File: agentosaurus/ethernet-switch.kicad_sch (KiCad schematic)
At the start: 19 parts, among them T1 HX1188NL, U1 RTL8367S, Y1 25MHz

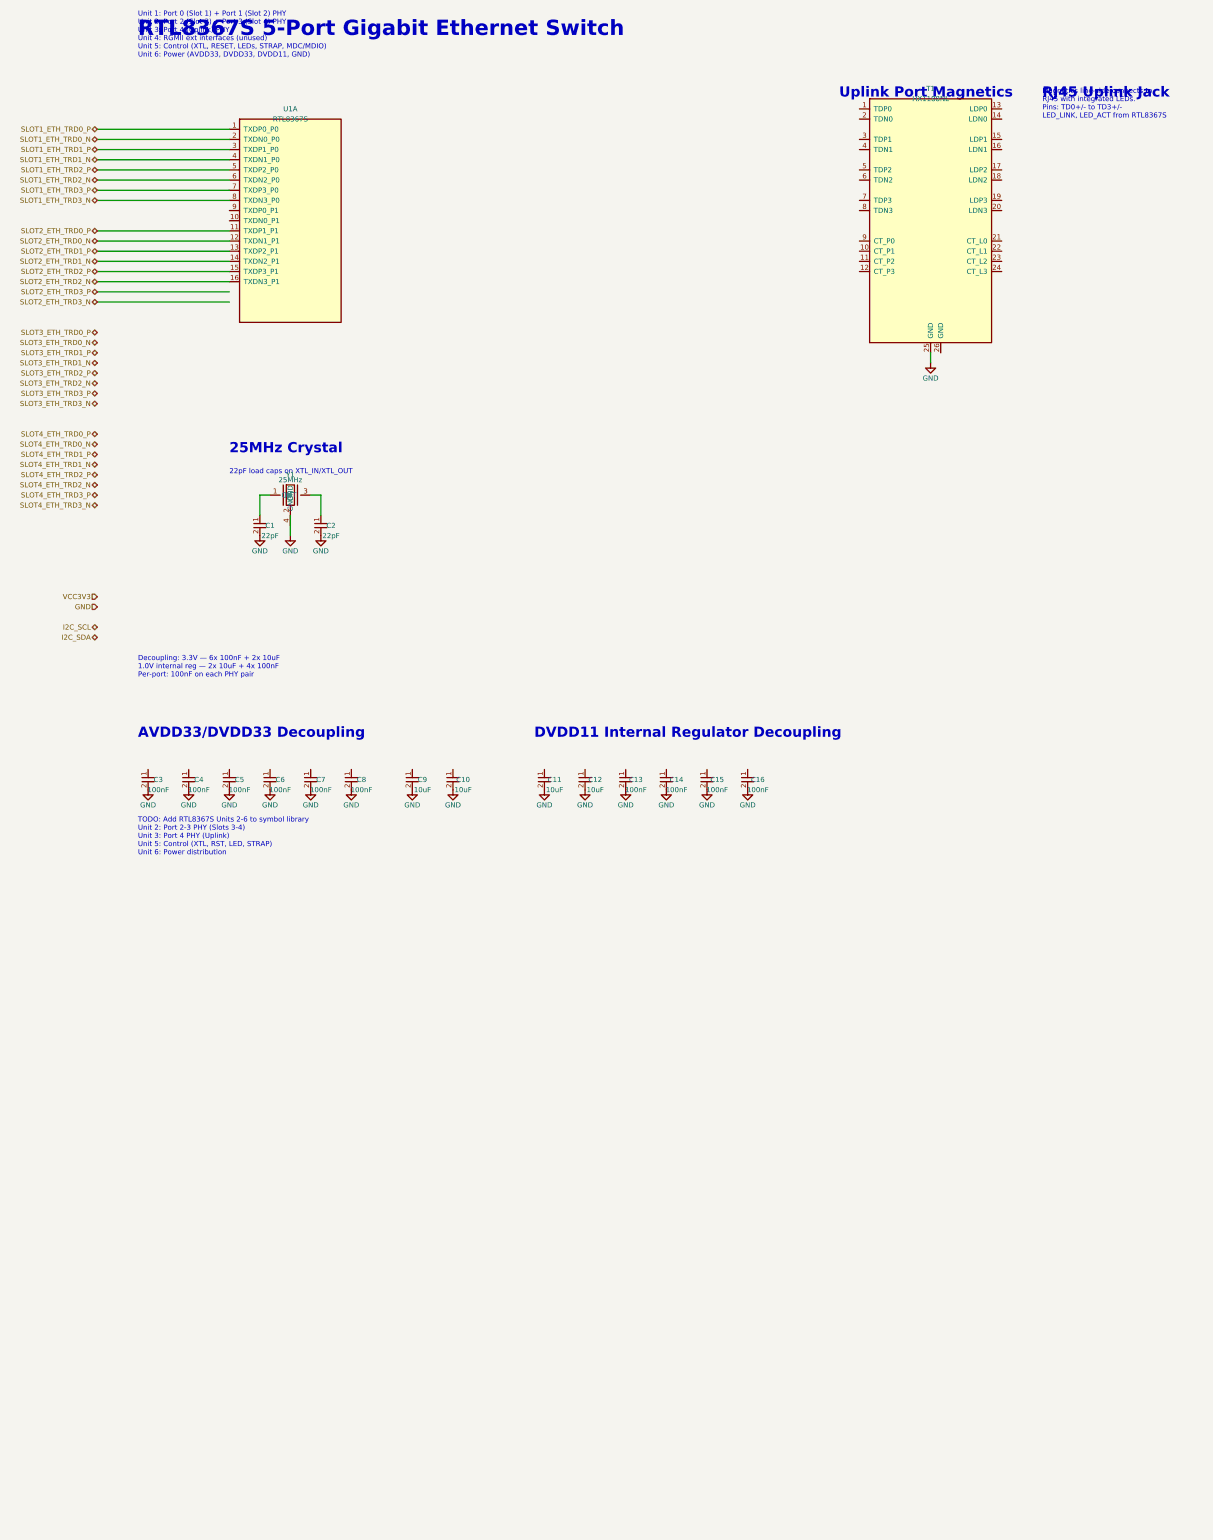
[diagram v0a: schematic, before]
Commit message: Add RTL8367S Units 2-6 with full wiring to ethernet switch
- Unit 2 (Ports 2-3 PHY): Slots 3-4 ethernet connections
- Unit 3 (Port 4 PHY): Uplink magnetics T1 connections
- Unit 5 (Control): MDC/MDIO to I2C, XTL to crystal, reset pull-up,
  strap pins to GND, MNG_MODE pull-up for SMI mode
- Unit 6 (Power): AVDD33/DVDD33 to VCC3V3, DVDD11 internal reg,
  AGND/DGND to GND
- Remove TODO text annotation

https://claude.ai/code/session_01UhhXLgEHsAy83XEALyNrDb
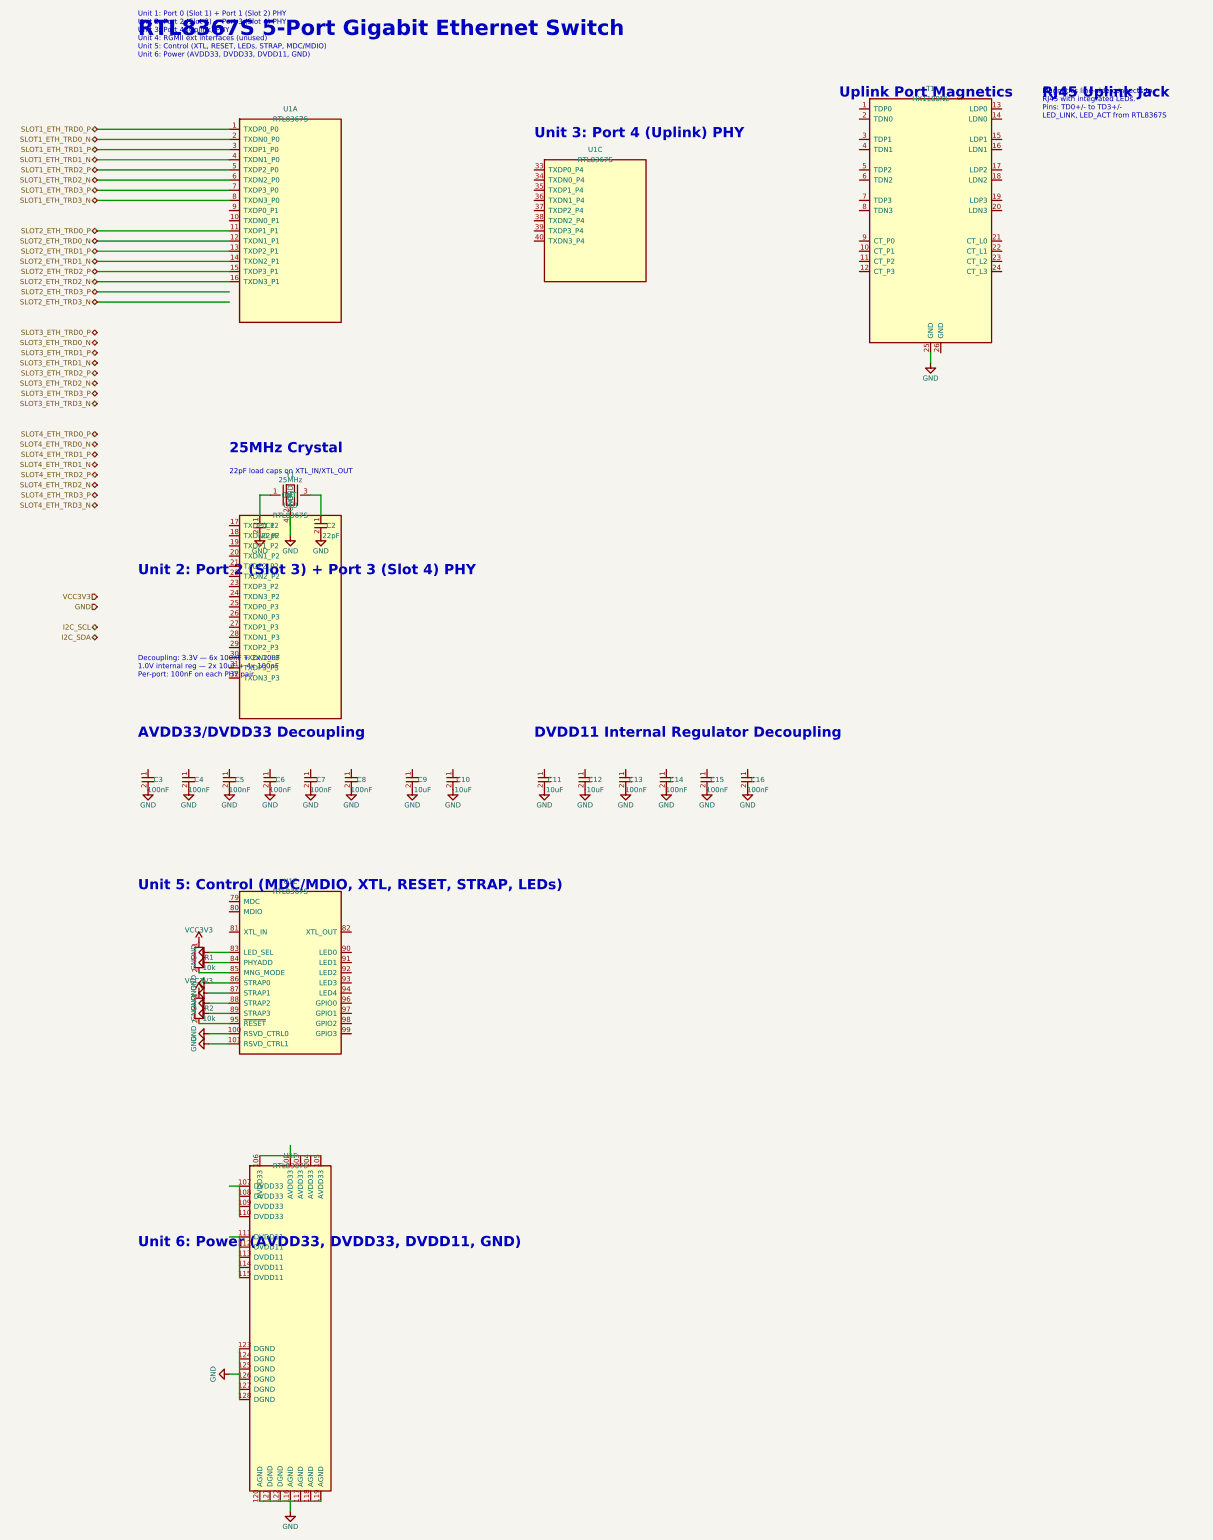
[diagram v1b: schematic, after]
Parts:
- added R1, R2: 10k, Resistor_SMD:R_0402_1005Metric, symbol Device:R
- added unit 2 of U1
- added unit 3 of U1
- added unit 5 of U1
- added unit 6 of U1
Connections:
- net GND: now also U1.100 (RSVD_CTRL0), U1.101 (RSVD_CTRL1), U1.116 (AGND), U1.83 (LED_SEL), U1.84 (PHYADD), U1.86 (STRAP0), U1.87 (STRAP1), U1.88 (STRAP2), U1.89 (STRAP3)
- net VCC3V3: now also R1.1, R2.1
- new net: R1.2, U1.85 (MNG_MODE)
- new net: R2.2, U1.95 (~{RESET})
- new net: U1.105 (AVDD33), U1.106 (AVDD33)
- new net: U1.107 (DVDD33), U1.110 (DVDD33)
- new net: U1.111 (DVDD11), U1.115 (DVDD11)
- new net: U1.119 (AGND), U1.120 (AGND)
- new net: U1.123 (DGND), U1.128 (DGND)
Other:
- note added: "Unit 2: Port 2 (Slot 3) + Port 3 (Slot 4) PHY"
- note added: "Unit 3: Port 4 (Uplink) PHY"
- note added: "Unit 5: Control (MDC/MDIO, XTL, RESET, STRAP, LEDs)"
- note added: "Unit 6: Power (AVDD33, DVDD33, DVDD11, GND)"
- note removed: "TODO: Add RTL8367S Units 2-6 to symbol library Unit 2: Port 2-3 PHY (Slots 3-4) Unit 3: Port 4 PHY (Uplink) Unit 5: Control (XTL, RST, LED, STRAP) Unit 6: Power distribution"
